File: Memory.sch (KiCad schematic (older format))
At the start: 25 parts, among them U10 74LS05, U11 74HCT00, U12 74LS27, U13 74HC74, U14 74HC86, U2 AS6C4008-55PCN, U3 AS6C4008-55PCN, U4 AS6C4008-55PCN, U5 AS6C4008-55PCN, U6 74HCT00, U7 74LS32, U8 74LS32, U9 74LS05

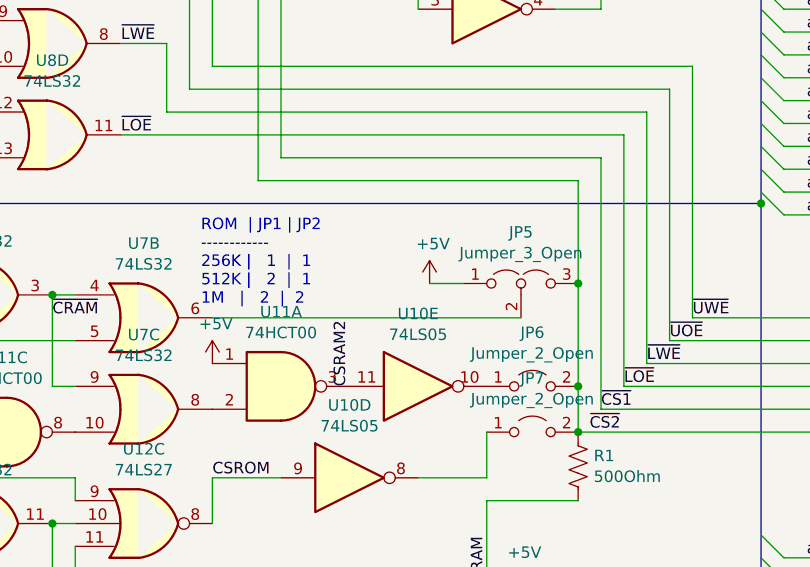
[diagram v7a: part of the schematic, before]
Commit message: wire the jumper up correctly
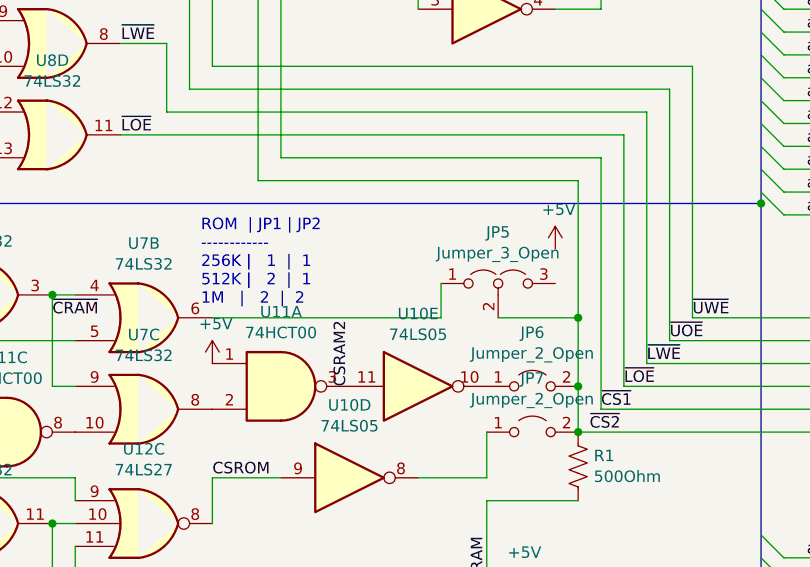
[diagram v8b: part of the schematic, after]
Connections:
- net +5V: no longer JP5.1 (A)
- net ~CS2: now also JP5.2 (C); no longer JP5.3 (B)
- net at U7.6: now also JP5.1 (A); no longer JP5.2 (C)
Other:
- moved on the sheet: JP5
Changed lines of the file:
@@
 Wire Wire Line
 	5500 2500 5500 3600
-Wire Wire Line
-	5400 2600 5400 3050
 $Comp
 L jumper:Jumper_2_Open JP6
@@
 L jumper:Jumper_3_Open JP5
 U 1 1 602480DF
-P 5150 3050
-F 0 "JP5" H 5150 3274 50  0000 C CNN
-F 1 "Jumper_3_Open" H 5150 3183 50  0000 C CNN
-F 2 "" H 5150 3050 50  0001 C CNN
-F 3 "~" H 5150 3050 50  0001 C CNN
-	1    5150 3050
+P 5050 3050
+F 0 "JP5" H 5050 3274 50  0000 C CNN
+F 1 "Jumper_3_Open" H 5050 3183 50  0000 C CNN
+F 2 "" H 5050 3050 50  0001 C CNN
+F 3 "~" H 5050 3050 50  0001 C CNN
+	1    5050 3050
 	1    0    0    -1
 $EndComp
-Connection ~ 5400 3050
 Wire Wire Line
-	5400 3050 5400 3500
-Wire Wire Line
-	3800 3200 5150 3200
+	3800 3200 4800 3200
 $Comp
 L OpenAmiga2000CoproAdapter-rescue:+5V-power #PWR?
 U 1 1 6026A4ED
-P 4750 3050
+P 5300 2900
 AR Path="/6026A4ED" Ref="#PWR?"  Part="1"
 AR Path="/6068F728/6026A4ED" Ref="#PWR0123"  Part="1"
-F 0 "#PWR0123" H 4750 2900 50  0001 C CNN
-F 1 "+5V" H 4765 3223 50  0000 C CNN
-F 2 "" H 4750 3050 50  0001 C CNN
-F 3 "" H 4750 3050 50  0001 C CNN
-	1    4750 3050
+F 0 "#PWR0123" H 5300 2750 50  0001 C CNN
+F 1 "+5V" H 5315 3073 50  0000 C CNN
+F 2 "" H 5300 2900 50  0001 C CNN
+F 3 "" H 5300 2900 50  0001 C CNN
+	1    5300 2900
 	1    0    0    -1
 $EndComp
-Wire Wire Line
-	4750 3050 4900 3050
 Wire Wire Line
 	700  1100 2700 1100
@@
 Wire Wire Line
 	3100 4100 3100 4600
+Connection ~ 2500 3000
+Wire Wire Line
+	2500 3000 2500 4000
+Wire Wire Line
+	5050 3200 5400 3200
+Wire Wire Line
+	4800 3050 4800 3200
+Connection ~ 5400 3200
+Wire Wire Line
+	5400 3200 5400 3500
+Wire Wire Line
+	5400 2600 5400 3200
 Wire Bus Line
 	900  2700 900  4350
@@
 Wire Bus Line
 	8900 600  8900 5950
-Connection ~ 2500 3000
-Wire Wire Line
-	2500 3000 2500 4000
 $EndSCHEMATC
